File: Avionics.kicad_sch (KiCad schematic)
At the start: 0 parts

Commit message: Add RP2350 (and onboarding I guess)
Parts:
- added U3: RP2350B-QFN80, RP2350X:RP2350B_QFN-80_EP_10.573x10.573_Pitch0.4mm, symbol rp2350b-qfn80:RP2350B-QFN80
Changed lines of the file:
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@@
 	(generator_version "9.0")
 	(paper "A4")
+	(symbol
+		(lib_id "rp2350b-qfn80:RP2350B-QFN80")
+		(at 132.08 96.52 0)
+		(unit 1)
+		(exclude_from_sim no)
+		(in_bom yes)
+		(on_board yes)
+		(dnp no)
+		(fields_autoplaced yes)
+		(property "Reference" "U3"
+			(at 134.2233 173.99 0)
+			(effects
+				(font
+					(size 1.27 1.27)
+				)
+				(justify left)
+			)
+		)
+		(property "Value" "RP2350B-QFN80"
+			(at 134.2233 176.53 0)
+			(effects
+				(font
+					(size 1.27 1.27)
+				)
+				(justify left)
+			)
+		)
+		(property "Footprint" "RP2350X:RP2350B_QFN-80_EP_10.573x10.573_Pitch0.4mm"
+			(at 125.73 50.8 0)
+			(effects
+				(font
+					(size 1.27 1.27)
+				)
+				(hide yes)
+			)
+		)
+		(property "Datasheet" ""
+			(at 125.73 50.8 0)
+			(effects
+				(font
+					(size 1.27 1.27)
+				)
+				(hide yes)
+			)
+		)
+		(property "Description" ""
+			(at 130.81 54.61 0)
+			(effects
+				(font
+					(size 1.27 1.27)
+				)
+				(hide yes)
+			)
+		)
+		(pin "4"
+		)
+		(pin "7"
+		)
+		(pin "9"
+		)
+		(pin "24"
+		)
+		(pin "80"
+		)
+		(pin "66"
+		)
+		(pin "78"
+		)
+		(pin "2"
+		)
+		(pin "60"
+		)
+		(pin "50"
+		)
+		(pin "59"
+		)
+		(pin "41"
+		)
+		(pin "29"
+		)
+		(pin "77"
+		)
+		(pin "68"
+		)
+		(pin "15"
+		)
+		(pin "5"
+		)
+		(pin "79"
+		)
+		(pin "1"
+		)
+		(pin "76"
+		)
+		(pin "3"
+		)
+		(pin "67"
+		)
+		(pin "6"
+		)
+		(pin "8"
+		)
+		(pin "25"
+		)
+		(pin "44"
+		)
+		(pin "18"
+		)
+		(pin "14"
+		)
+		(pin "36"
+		)
+		(pin "52"
+		)
+		(pin "43"
+		)
+		(pin "42"
+		)
+		(pin "47"
+		)
+		(pin "26"
+		)
+		(pin "27"
+		)
+		(pin "39"
+		)
+		(pin "11"
+		)
+		(pin "16"
+		)
+		(pin "13"
+		)
+		(pin "20"
+		)
+		(pin "28"
+		)
+		(pin "21"
+		)
+		(pin "38"
+		)
+		(pin "22"
+		)
+		(pin "37"
+		)
+		(pin "19"
+		)
+		(pin "12"
+		)
+		(pin "17"
+		)
+		(pin "23"
+		)
+		(pin "40"
+		)
+		(pin "45"
+		)
+		(pin "46"
+		)
+		(pin "48"
+		)
+		(pin "49"
+		)
+		(pin "53"
+		)
+		(pin "54"
+		)
+		(pin "55"
+		)
+		(pin "56"
+		)
+		(pin "57"
+		)
+		(pin "58"
+		)
+		(pin "34"
+		)
+		(pin "72"
+		)
+		(pin "65"
+		)
+		(pin "75"
+		)
+		(pin "35"
+		)
+		(pin "32"
+		)
+		(pin "70"
+		)
+		(pin "31"
+		)
+		(pin "63"
+		)
+		(pin "64"
+		)
+		(pin "62"
+		)
+		(pin "73"
+		)
+		(pin "51"
+		)
+		(pin "81"
+		)
+		(pin "30"
+		)
+		(pin "61"
+		)
+		(pin "71"
+		)
+		(pin "10"
+		)
+		(pin "74"
+		)
+		(pin "69"
+		)
+		(pin "33"
+		)
+		(instances
+			(project ""
+				(path "/31ba118e-63c6-4589-abeb-d0c379bb13c1/c6c9b9a9-ddbf-445b-97cd-a6e878077684"
+					(reference "U3")
+					(unit 1)
+				)
+			)
+		)
+	)
 )

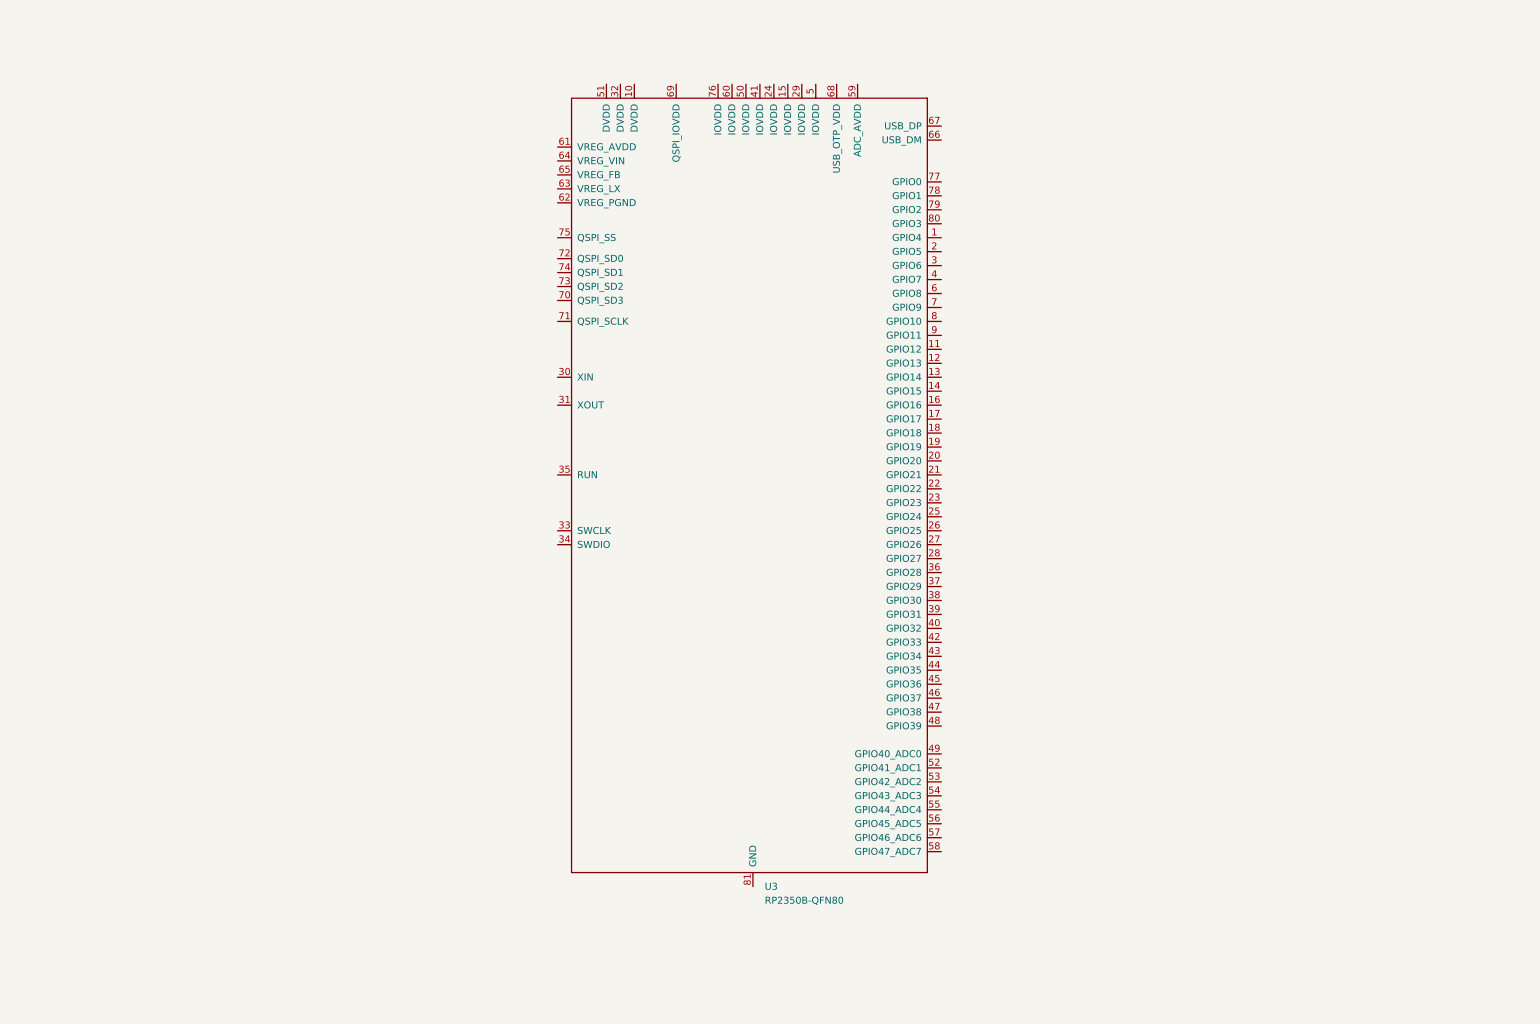
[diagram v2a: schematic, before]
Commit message: RP2350 Scheme
Added RP2350B schematic to Avionics sub schematic. Added hierarchy schematics for each of the sub schematics for the RP2350B and completed schematics for 4/6. The other 2 need objects to be added to a library to finish this part (JST Connector and Crystal).
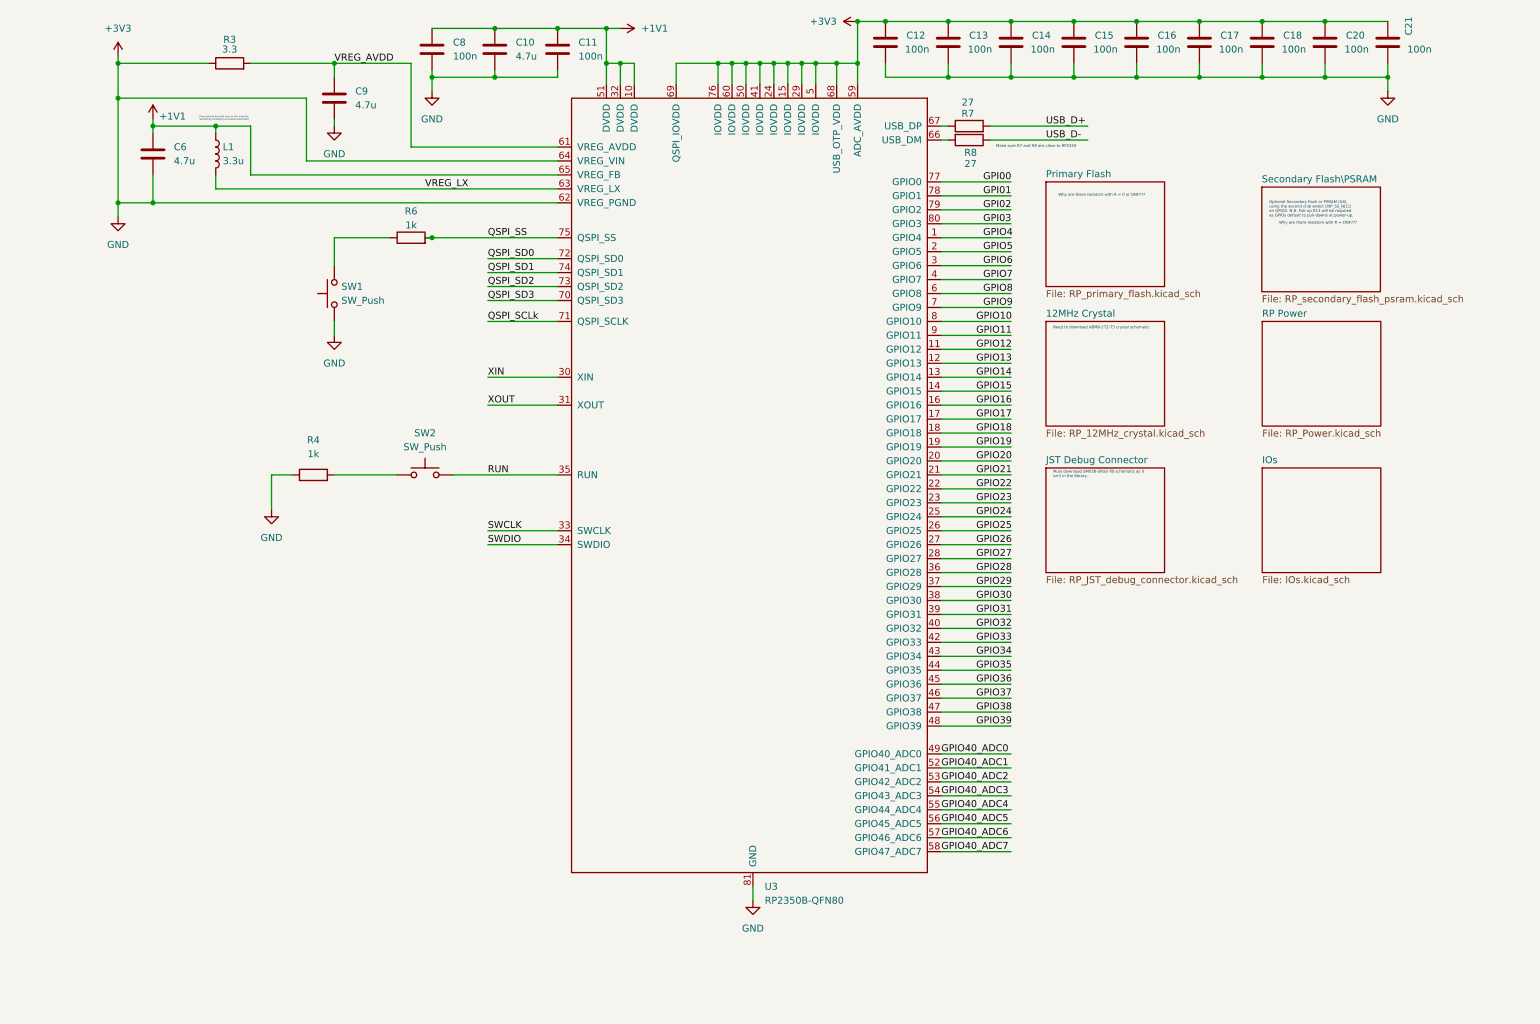
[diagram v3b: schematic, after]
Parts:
- added C10, C6, C9: 4.7u, symbol Device:C
- added C11, C12, C13, C14, C15, C16, C17, C18, C20, C21, C8: 100n, symbol Device:C
- added L1: 3.3u, symbol Device:L
- added R3: 3.3, symbol Device:R
- added R4, R6: 1k, symbol Device:R
- added R7, R8: 27, symbol Device:R
- added SW1, SW2: SW_Push, symbol Switch:SW_Push
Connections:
- net GPIO4: now reaches U3.1 (GPIO4)
- net +1V1: now reaches U3.10 (DVDD)
- net +1V1: now also U3.32 (DVDD), U3.51 (DVDD), U3.65 (VREG_FB), C10.1, C11.1, C6.1, C8.1, L1.1
- net GPIO12: now reaches U3.11 (GPIO12)
- net GPIO13: now reaches U3.12 (GPIO13)
- net GPIO14: now reaches U3.13 (GPIO14)
- net GPIO15: now reaches U3.14 (GPIO15)
- net +3V3: now reaches U3.15 (IOVDD)
- net +3V3: now also U3.24 (IOVDD), U3.29 (IOVDD), U3.41 (IOVDD), U3.5 (IOVDD), U3.50 (IOVDD), U3.59 (ADC_AVDD), U3.60 (IOVDD), U3.62 (VREG_PGND), U3.64 (VREG_VIN), U3.68 (USB_OTP_VDD), U3.69 (QSPI_IOVDD), U3.76 (IOVDD), U3.81 (GND), C10.2, C11.2, C12.1, C12.2, C13.1, C13.2, C14.1, C14.2, C15.1, C15.2, C16.1, C16.2, C17.1, C17.2, C18.1, C18.2, C20.1, C20.2, C21.1, C21.2, C6.2, C8.2, C9.2, R3.1, R4.1, SW1.1
- net GPIO16: now reaches U3.16 (GPIO16)
- net GPIO17: now reaches U3.17 (GPIO17)
- net GPIO18: now reaches U3.18 (GPIO18)
- net GPIO19: now reaches U3.19 (GPIO19)
- net GPIO5: now reaches U3.2 (GPIO5)
- net GPIO20: now reaches U3.20 (GPIO20)
- net GPIO21: now reaches U3.21 (GPIO21)
- net GPIO22: now reaches U3.22 (GPIO22)
- net GPIO23: now reaches U3.23 (GPIO23)
- net GPIO24: now reaches U3.25 (GPIO24)
- net GPIO25: now reaches U3.26 (GPIO25)
- net GPIO26: now reaches U3.27 (GPIO26)
- net GPIO27: now reaches U3.28 (GPIO27)
- net GPIO6: now reaches U3.3 (GPIO6)
- net XIN: now reaches U3.30 (XIN)
- net XOUT: now reaches U3.31 (XOUT)
- net SWCLK: now reaches U3.33 (SWCLK)
- net SWDIO: now reaches U3.34 (SWDIO)
- net RUN: now reaches U3.35 (RUN)
- net RUN: now also SW2.2
- net GPIO28: now reaches U3.36 (GPIO28)
- net GPIO29: now reaches U3.37 (GPIO29)
- net GPIO30: now reaches U3.38 (GPIO30)
- net GPIO31: now reaches U3.39 (GPIO31)
- net GPIO7: now reaches U3.4 (GPIO7)
- net GPIO32: now reaches U3.40 (GPIO32)
- net GPIO33: now reaches U3.42 (GPIO33)
- net GPIO34: now reaches U3.43 (GPIO34)
- net GPIO35: now reaches U3.44 (GPIO35)
- net GPIO36: now reaches U3.45 (GPIO36)
- net GPIO37: now reaches U3.46 (GPIO37)
- net GPIO38: now reaches U3.47 (GPIO38)
- net GPIO39: now reaches U3.48 (GPIO39)
- net GPIO40_ADC0: now reaches U3.49 (GPIO40_ADC0)
- net GPIO40_ADC1: now reaches U3.52 (GPIO41_ADC1)
- net GPIO40_ADC2: now reaches U3.53 (GPIO42_ADC2)
- net GPIO40_ADC3: now reaches U3.54 (GPIO43_ADC3)
- net GPIO40_ADC4: now reaches U3.55 (GPIO44_ADC4)
- net GPIO40_ADC5: now reaches U3.56 (GPIO45_ADC5)
- net GPIO40_ADC6: now reaches U3.57 (GPIO46_ADC6)
- net GPIO40_ADC7: now reaches U3.58 (GPIO47_ADC7)
- net GPIO8: now reaches U3.6 (GPIO8)
- net VREG_AVDD: now reaches U3.61 (VREG_AVDD)
- net VREG_AVDD: now also C9.1, R3.2
- net VREG_LX: now reaches U3.63 (VREG_LX)
- net VREG_LX: now also L1.2
- net at U3.66 (USB_DM): now also R8.2
- net at U3.67 (USB_DP): now also R7.1
- net GPIO9: now reaches U3.7 (GPIO9)
- net QSPI_SD3: now reaches U3.70 (QSPI_SD3)
- net QSPI_SCLk: now reaches U3.71 (QSPI_SCLK)
- net QSPI_SD0: now reaches U3.72 (QSPI_SD0)
- net QSPI_SD2: now reaches U3.73 (QSPI_SD2)
- net QSPI_SD1: now reaches U3.74 (QSPI_SD1)
- net QSPI_SS: now reaches U3.75 (QSPI_SS)
- net QSPI_SS: now also R6.2
- net GPI00: now reaches U3.77 (GPIO0)
- net GPI01: now reaches U3.78 (GPIO1)
- net GPI02: now reaches U3.79 (GPIO2)
- net GPIO10: now reaches U3.8 (GPIO10)
- net GPI03: now reaches U3.80 (GPIO3)
- net GPIO11: now reaches U3.9 (GPIO11)
- new net: R6.1, SW1.2
- new net: R4.2, SW2.1
- new net USB_D+: R7.2
- new net USB_D-: R8.1
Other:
- added sheet 12MHz Crystal (RP_12MHz_crystal.kicad_sch)
- added sheet IOs (IOs.kicad_sch)
- added sheet JST Debug Connector (RP_JST_debug_connector.kicad_sch)
- added sheet Primary Flash (RP_primary_flash.kicad_sch)
- added sheet RP Power (RP_Power.kicad_sch)
- added sheet Secondary Flash\PSRAM (RP_secondary_flash_psram.kicad_sch)
- note added: "Make sure R7 and R8 are close to RP2350"
- note added: "Must download SM03B-SRSS-TB schematic as it isn't in the library."
- note added: "Need to download ABM8-272-T3 crystal schematic"
- note added: "Optional Secondary flash or PSRAM (U4), using the second chip select (XIP_SS_N[1]) on GPIO0. N.B. Pull-up R13 will be required as GPIOs default to pull-downs at power-up."
- note added: "There should be a dot next to this inductor. Something something should be polarized?"
- note added: "Why are there resistors with R = 0 or DNF???"
- note added: "Why are there resistors with R = DNF???"

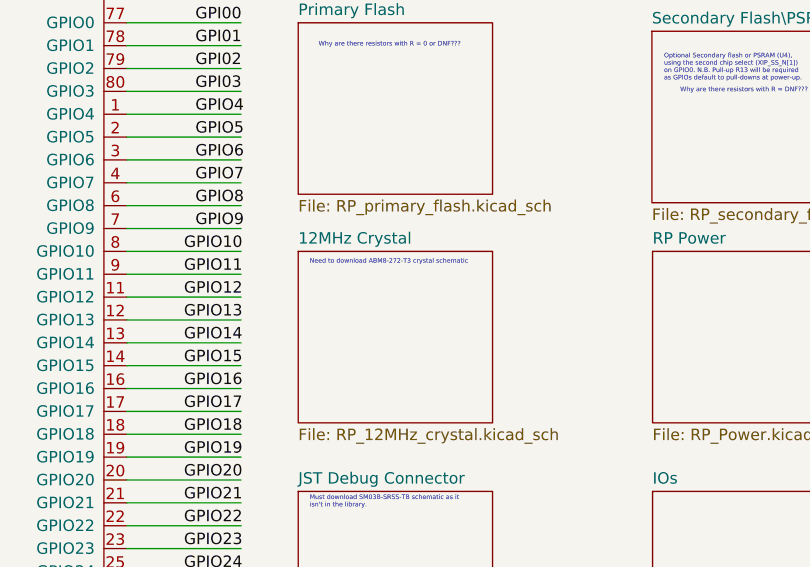
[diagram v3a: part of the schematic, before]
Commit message: Downloaded the Footprints for RP2350B
Downloaded the ABM8-272-T3 for the crystal and the SM03B-SRSS-TB for the JST connector, though the later is not correct (I think) because it lacks mechanical pads within the footprint.
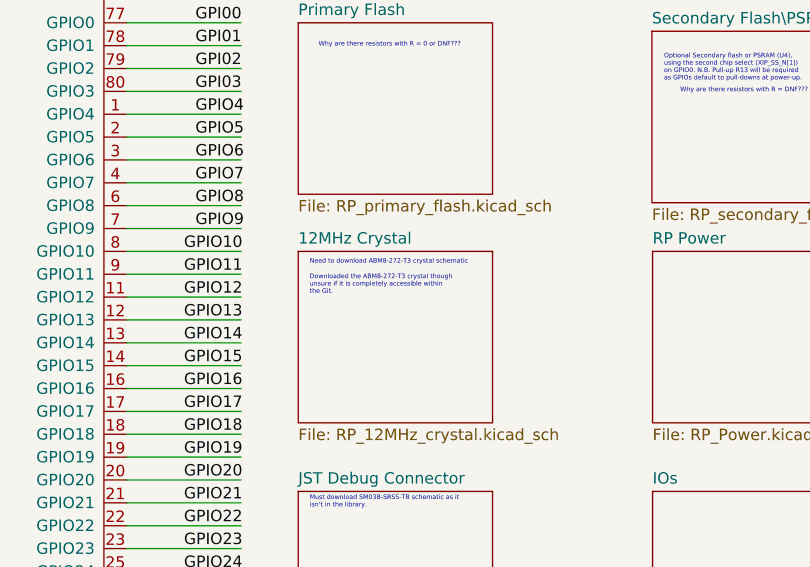
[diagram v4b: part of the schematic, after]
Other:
- note added: "Downloaded the ABM8-272-T3 crystal though unsure if it is completely accessible within the Git."
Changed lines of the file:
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@@
+		)
+	)
+	(text "Downloaded the ABM8-272-T3 crystal though \nunsure if it is completely accessible within \nthe Git."
+		(exclude_from_sim no)
+		(at 186.69 74.93 0)
+		(effects
+			(font
+				(size 0.508 0.508)
+				(color 43 47 255 1)
+			)
+			(justify left)
 		)
 	)
